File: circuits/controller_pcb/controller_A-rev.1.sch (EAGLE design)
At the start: 54 parts, among them IC1 DS1820, J3 USB-MICROB", Q2 FDN340P, Q3 SI2333DS, Q5 BSS138, U1 ATMEGA328P_TQFP, U2 MIC5219 5V

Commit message: Updated controller Version A to Revision 1 - UNTESTED
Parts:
- renumbered U$1 to U5, U$10 to U8, U$2 to U3, U$3 to U6, U$4 to U7, U$5 to U9, U$6 to X1, U$8 to U4, U$9 to X2
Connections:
- net N$7 renamed AUX

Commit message: Updated Q1 and replaced schottky diode - UNTESTED
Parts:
- removed D1: IN5819, SparkFun-DiscreteSemi:MBRA140
- removed J3: USB-MICROB", SparkFun-Connectors:USB-MICROB"
- removed Q5: BSS138, transistor-fet:BSS138
- added J1: (no value), ch340g:USB_MICROB_PLUGNOHOLES
- added Q1: FDN340P, transistor-fet:FDN340P
- added Z1: BAT41KFILM, schottky:BAT41KFILM
- C11: value 100n -> 1u
- RN1, RN2: value (none) -> 1k
- TP1, TP2: value PTR1TP12R -> PTR1TP10R; device testpad:PTR1TP12R -> testpad:PTR1TP10R
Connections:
- net 5V: now also R5.1
- net D+: now also J1.D+; no longer J3.D+
- net D-: now also J1.D-; no longer J3.D-
- net DATA: now also Q1.D, Z1.1; no longer D1.A, Q5.D
- net DIR: now also Q1.G; no longer Q5.G
- net GND: now also J1.GND, J1.SHIELD; no longer J3.GND, J3.SHIELD, R5.1
- net N$10: now also J1.VCC; no longer J3.VBUS
- net RX: now also Q1.S; no longer Q5.S
- net TX: now also Z1.2; no longer D1.C
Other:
- moved on the sheet: R5, R6

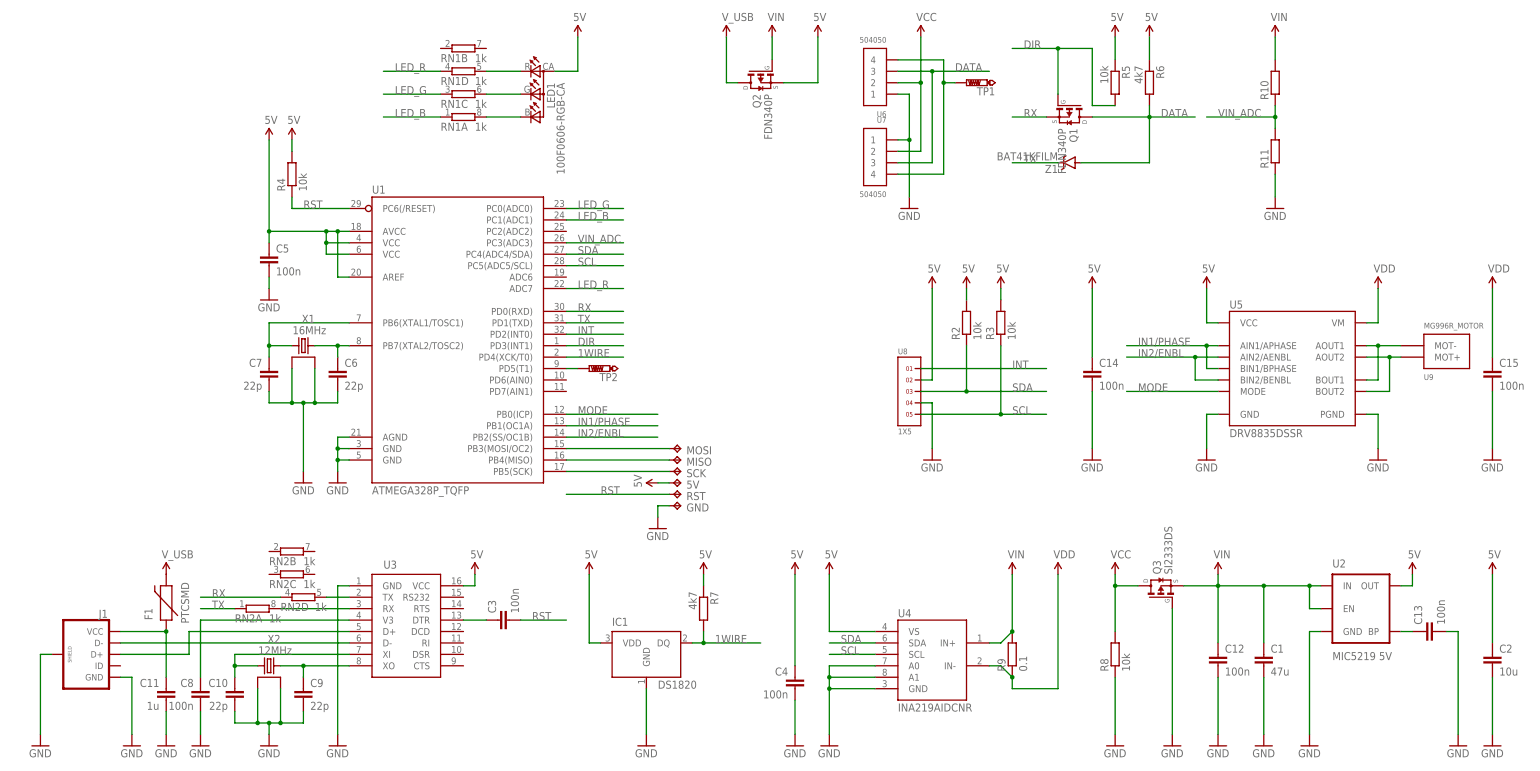
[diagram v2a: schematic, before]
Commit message: Updated controller PCB - Tested and working
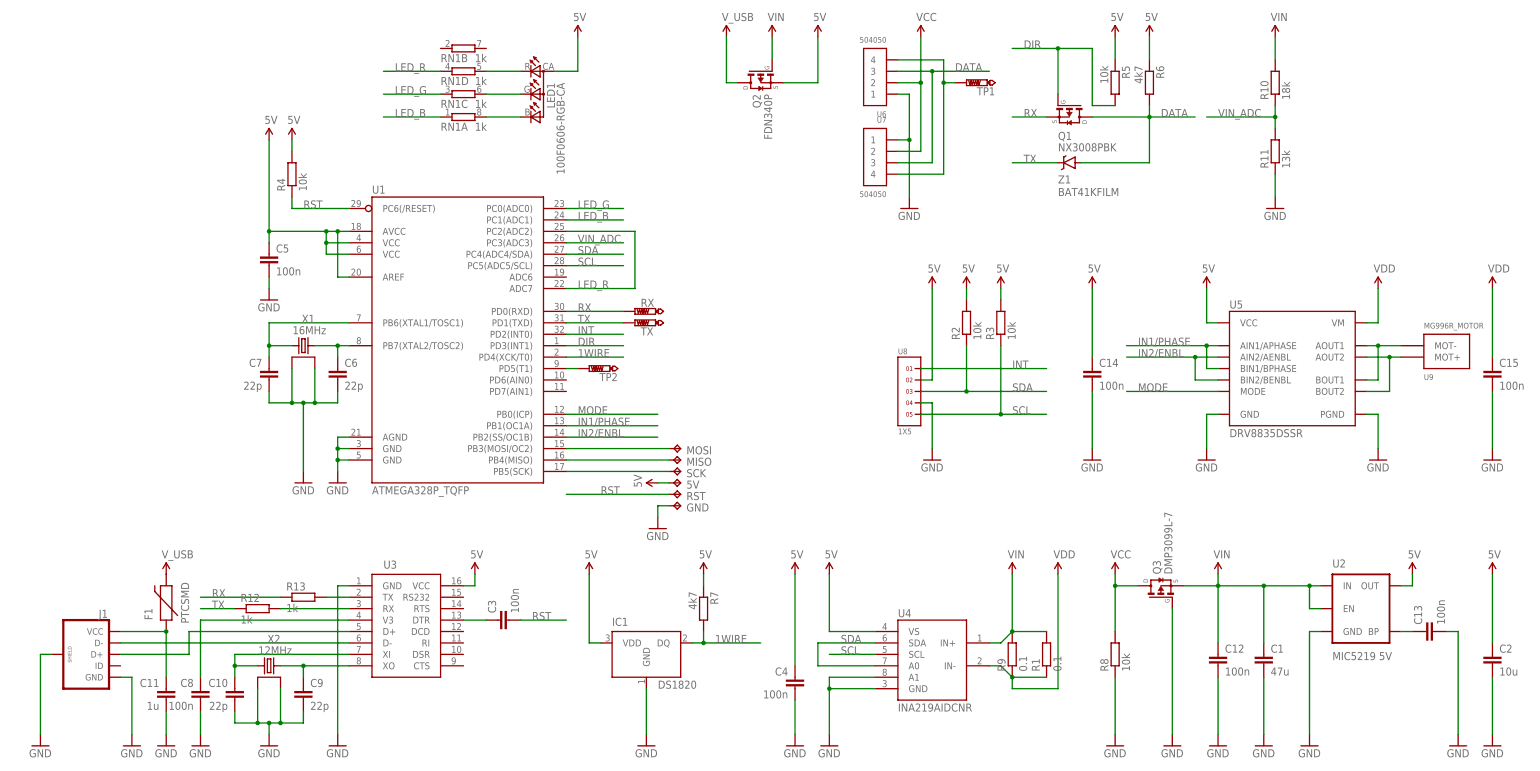
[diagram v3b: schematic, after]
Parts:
- removed RN2: 1k, resistor-dil:4R-NYC124
- added R1: 0.1, rcl:R-EU_R0603
- added R12, R13: 1k, rcl:R-EU_R0402
- added RX, TX: PTR1TP10R, testpad:PTR1TP10R
- J1: device ch340g:USB_MICROB_PLUGNOHOLES -> ch340g:USB_MICROB_PLUGCONN-11752
- Q1: value FDN340P -> NX3008PBK
- Q3: value SI2333DS -> DMP3099L-7
- R10: value (none) -> 18k
- R11: value (none) -> 13k
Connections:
- net GND: no longer U4.A0
- net LED_R: now also U1.PC2(ADC2)
- net N$15: now also R12.2; no longer RN2A.2
- net N$6: now also R13.2; no longer RN2D.2
- net RX: now also R13.1, RX.TP; no longer RN2D.1
- net SDA: now also U4.A0
- net TX: now also R12.1, TX.TP; no longer RN2A.1
- net VDD: now also R1.1
- net VIN: now also R1.2
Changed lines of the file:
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@@
 <part name="GND14" library="SparkFun-Aesthetics" deviceset="GND" device=""/>
 <part name="SUPPLY20" library="SparkFun-Aesthetics" deviceset="VDD" device=""/>
-<part name="Q3" library="transistor-fet" deviceset="SI2333DS" device=""/>
+<part name="Q3" library="transistor-fet" deviceset="SI2333DS" device="" value="DMP3099L-7"/>
 <part name="SUPPLY21" library="SparkFun-Aesthetics" deviceset="VIN" device=""/>
 <part name="R8" library="rcl" deviceset="R-EU_" device="R0402" value="10k"/>
@@
 <part name="SUPPLY26" library="SparkFun-Aesthetics" deviceset="5V" device=""/>
 <part name="GND24" library="SparkFun-Aesthetics" deviceset="GND" device=""/>
-<part name="R10" library="rcl" deviceset="R-EU_" device="R0402"/>
-<part name="R11" library="rcl" deviceset="R-EU_" device="R0402"/>
+<part name="R10" library="rcl" deviceset="R-EU_" device="R0402" value="18k"/>
+<part name="R11" library="rcl" deviceset="R-EU_" device="R0402" value="13k"/>
 <part name="SUPPLY30" library="SparkFun-Aesthetics" deviceset="VIN" device=""/>
 <part name="GND26" library="SparkFun-Aesthetics" deviceset="GND" device=""/>
@@
 <part name="SUPPLY14" library="SparkFun-Aesthetics" deviceset="5V" device=""/>
 <part name="U8" library="headers(.05in)" deviceset="1X5" device=""/>
-<part name="RN2" library="resistor-dil" deviceset="4R-N" device="YC124" value="1k"/>
 <part name="TP1" library="testpad" deviceset="PTR1" device="TP10R" value="PTR1TP10R"/>
 <part name="TP2" library="testpad" deviceset="PTR1" device="TP10R" value="PTR1TP10R"/>
-<part name="J1" library="ch340g" deviceset="USB_MICROB_PLUG" device="NOHOLES"/>
+<part name="J1" library="ch340g" deviceset="USB_MICROB_PLUG" device="CONN-11752"/>
 <part name="GND28" library="SparkFun-Aesthetics" deviceset="GND" device=""/>
-<part name="Q1" library="transistor-fet" deviceset="FDN340P" device=""/>
+<part name="Q1" library="transistor-fet" deviceset="FDN340P" device="" value="NX3008PBK"/>
 <part name="SUPPLY29" library="SparkFun-Aesthetics" deviceset="5V" device=""/>
 <part name="Z1" library="schottky" deviceset="BAT41KFILM" device=""/>
+<part name="R1" library="rcl" deviceset="R-EU_" device="R0603" value="0.1"/>
+<part name="R12" library="rcl" deviceset="R-EU_" device="R0402" value="1k"/>
+<part name="R13" library="rcl" deviceset="R-EU_" device="R0402" value="1k"/>
+<part name="RX" library="testpad" deviceset="PTR1" device="TP10R" value="PTR1TP10R"/>
+<part name="TX" library="testpad" deviceset="PTR1" device="TP10R" value="PTR1TP10R"/>
 </parts>
 <sheets>
@@
 <instance part="SUPPLY14" gate="G$1" x="76.2" y="27.94"/>
 <instance part="U8" gate="G$1" x="172.72" y="68.58"/>
-<instance part="RN2" gate="A" x="27.94" y="20.32"/>
-<instance part="RN2" gate="B" x="35.56" y="33.02"/>
-<instance part="RN2" gate="C" x="35.56" y="27.94"/>
-<instance part="RN2" gate="D" x="38.1" y="22.86"/>
 <instance part="TP1" gate="G$1" x="185.42" y="137.16" rot="R90"/>
 <instance part="TP2" gate="G$1" x="101.6" y="73.66" rot="R90"/>
 <instance part="J1" gate="G$1" x="-10.16" y="10.16" rot="MR0"/>
 <instance part="GND28" gate="1" x="-20.32" y="-10.16"/>
-<instance part="Q1" gate="G$1" x="208.28" y="129.54" rot="R270"/>
+<instance part="Q1" gate="G$1" x="208.28" y="129.54" smashed="yes" rot="R270">
+<attribute name="VALUE" x="205.74" y="121.92" size="1.778" layer="96"/>
+<attribute name="NAME" x="205.74" y="124.46" size="1.778" layer="95"/>
+</instance>
 <instance part="SUPPLY29" gate="G$1" x="218.44" y="147.32"/>
-<instance part="Z1" gate="G$1" x="208.28" y="119.38" rot="R180"/>
+<instance part="Z1" gate="G$1" x="208.28" y="119.38" smashed="yes" rot="R180">
+<attribute name="NAME" x="205.74" y="114.7826" size="1.778" layer="95"/>
+<attribute name="VALUE" x="205.74" y="111.9886" size="1.778" layer="96"/>
+</instance>
+<instance part="R1" gate="G$1" x="203.2" y="10.16" rot="R90"/>
+<instance part="R12" gate="G$1" x="27.94" y="20.32"/>
+<instance part="R13" gate="G$1" x="38.1" y="22.86"/>
+<instance part="RX" gate="G$1" x="111.76" y="86.36" smashed="yes" rot="R90">
+<attribute name="NAME" x="113.03" y="87.376" size="1.778" layer="95"/>
+<attribute name="TP_SIGNAL_NAME" x="114.3" y="87.63" size="1.778" layer="97" rot="R90"/>
+</instance>
+<instance part="TX" gate="G$1" x="111.76" y="83.82" smashed="yes" rot="R90">
+<attribute name="NAME" x="113.03" y="82.804" size="1.778" layer="95" rot="MR180"/>
+<attribute name="TP_SIGNAL_NAME" x="114.3" y="85.09" size="1.778" layer="97" rot="R90"/>
+</instance>
 </instances>
 <busses>
@@
 <segment>
 <pinref part="U4" gate="G$1" pin="SDA"/>
-<wire x1="165.1" y1="12.7" x2="154.94" y2="12.7" width="0.1524" layer="91"/>
+<wire x1="165.1" y1="12.7" x2="152.4" y2="12.7" width="0.1524" layer="91"/>
 <label x="157.48" y="12.7" size="1.778" layer="95"/>
+<pinref part="U4" gate="G$1" pin="A0"/>
+<wire x1="165.1" y1="7.62" x2="152.4" y2="7.62" width="0.1524" layer="91"/>
+<wire x1="152.4" y1="7.62" x2="152.4" y2="12.7" width="0.1524" layer="91"/>
 </segment>
 </net>
@@
 </segment>
 <segment>
-<pinref part="U4" gate="G$1" pin="A0"/>
 <pinref part="GND14" gate="1" pin="GND"/>
-<wire x1="165.1" y1="7.62" x2="154.94" y2="7.62" width="0.1524" layer="91"/>
-<wire x1="154.94" y1="7.62" x2="154.94" y2="5.08" width="0.1524" layer="91"/>
 <pinref part="U4" gate="G$1" pin="A1"/>
 <wire x1="154.94" y1="5.08" x2="154.94" y2="2.54" width="0.1524" layer="91"/>
 <wire x1="154.94" y1="2.54" x2="154.94" y2="-7.62" width="0.1524" layer="91"/>
 <wire x1="165.1" y1="5.08" x2="154.94" y2="5.08" width="0.1524" layer="91"/>
-<junction x="154.94" y="5.08"/>
 <pinref part="U4" gate="G$1" pin="GND"/>
 <wire x1="165.1" y1="2.54" x2="154.94" y2="2.54" width="0.1524" layer="91"/>
@@
 <wire x1="96.52" y1="86.36" x2="109.22" y2="86.36" width="0.1524" layer="91"/>
 <label x="99.06" y="86.36" size="1.778" layer="95"/>
+<pinref part="RX" gate="G$1" pin="TP"/>
 </segment>
 <segment>
 <wire x1="33.02" y1="22.86" x2="15.24" y2="22.86" width="0.1524" layer="91"/>
 <label x="17.78" y="22.86" size="1.778" layer="95"/>
-<pinref part="RN2" gate="D" pin="1"/>
+<pinref part="R13" gate="G$1" pin="1"/>
 </segment>
 </net>
@@
 <wire x1="96.52" y1="83.82" x2="109.22" y2="83.82" width="0.1524" layer="91"/>
 <label x="99.06" y="83.82" size="1.778" layer="95"/>
+<pinref part="TX" gate="G$1" pin="TP"/>
 </segment>
 <segment>
 <wire x1="22.86" y1="20.32" x2="15.24" y2="20.32" width="0.1524" layer="91"/>
 <label x="17.78" y="20.32" size="1.778" layer="95"/>
-<pinref part="RN2" gate="A" pin="1"/>
+<pinref part="R12" gate="G$1" pin="1"/>
 </segment>
 </net>
@@
 <junction x="195.58" y="15.24"/>
 <pinref part="R9" gate="G$1" pin="2"/>
+<pinref part="R1" gate="G$1" pin="2"/>
+<wire x1="203.2" y1="15.24" x2="195.58" y2="15.24" width="0.1524" layer="91"/>
 </segment>
 <segment>
@@
 <segment>
 <pinref part="U1" gate="U$1" pin="ADC7"/>
-<wire x1="96.52" y1="91.44" x2="109.22" y2="91.44" width="0.1524" layer="91"/>
+<wire x1="96.52" y1="91.44" x2="111.76" y2="91.44" width="0.1524" layer="91"/>
 <label x="99.06" y="91.44" size="1.778" layer="95"/>
+<wire x1="111.76" y1="91.44" x2="111.76" y2="104.14" width="0.1524" layer="91"/>
+<pinref part="U1" gate="U$1" pin="PC2(ADC2)"/>
+<wire x1="111.76" y1="104.14" x2="96.52" y2="104.14" width="0.1524" layer="91"/>
 </segment>
 </net>
@@
 <wire x1="205.74" y1="2.54" x2="205.74" y2="27.94" width="0.1524" layer="91"/>
 <pinref part="R9" gate="G$1" pin="1"/>
+<pinref part="R1" gate="G$1" pin="1"/>
+<wire x1="203.2" y1="5.08" x2="195.58" y2="5.08" width="0.1524" layer="91"/>
 </segment>
 <segment>
@@
 <pinref part="U3" gate="G$1" pin="TX"/>
 <wire x1="43.18" y1="22.86" x2="48.26" y2="22.86" width="0.1524" layer="91"/>
-<pinref part="RN2" gate="D" pin="2"/>
+<pinref part="R13" gate="G$1" pin="2"/>
 </segment>
 </net>
@@
 <pinref part="U3" gate="G$1" pin="RX"/>
 <wire x1="33.02" y1="20.32" x2="48.26" y2="20.32" width="0.1524" layer="91"/>
-<pinref part="RN2" gate="A" pin="2"/>
-</segment>
-</net>
+<pinref part="R12" gate="G$1" pin="2"/>
+</segment>
+</net>
